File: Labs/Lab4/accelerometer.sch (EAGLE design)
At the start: 15 parts

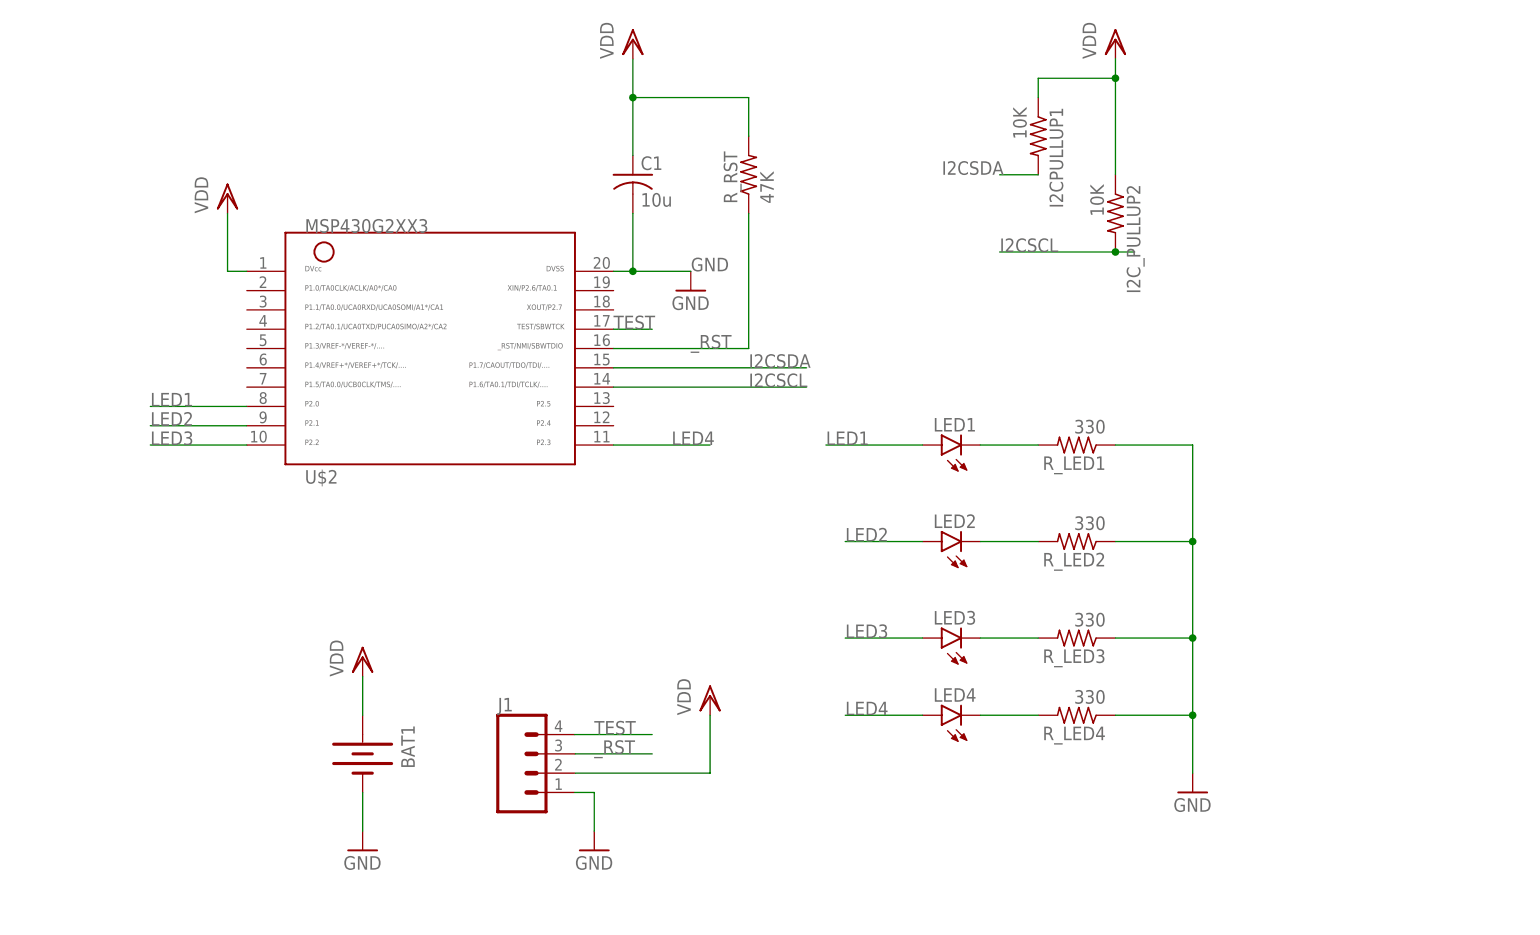
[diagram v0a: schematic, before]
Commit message: Fixed connections in Lab 4 schematic
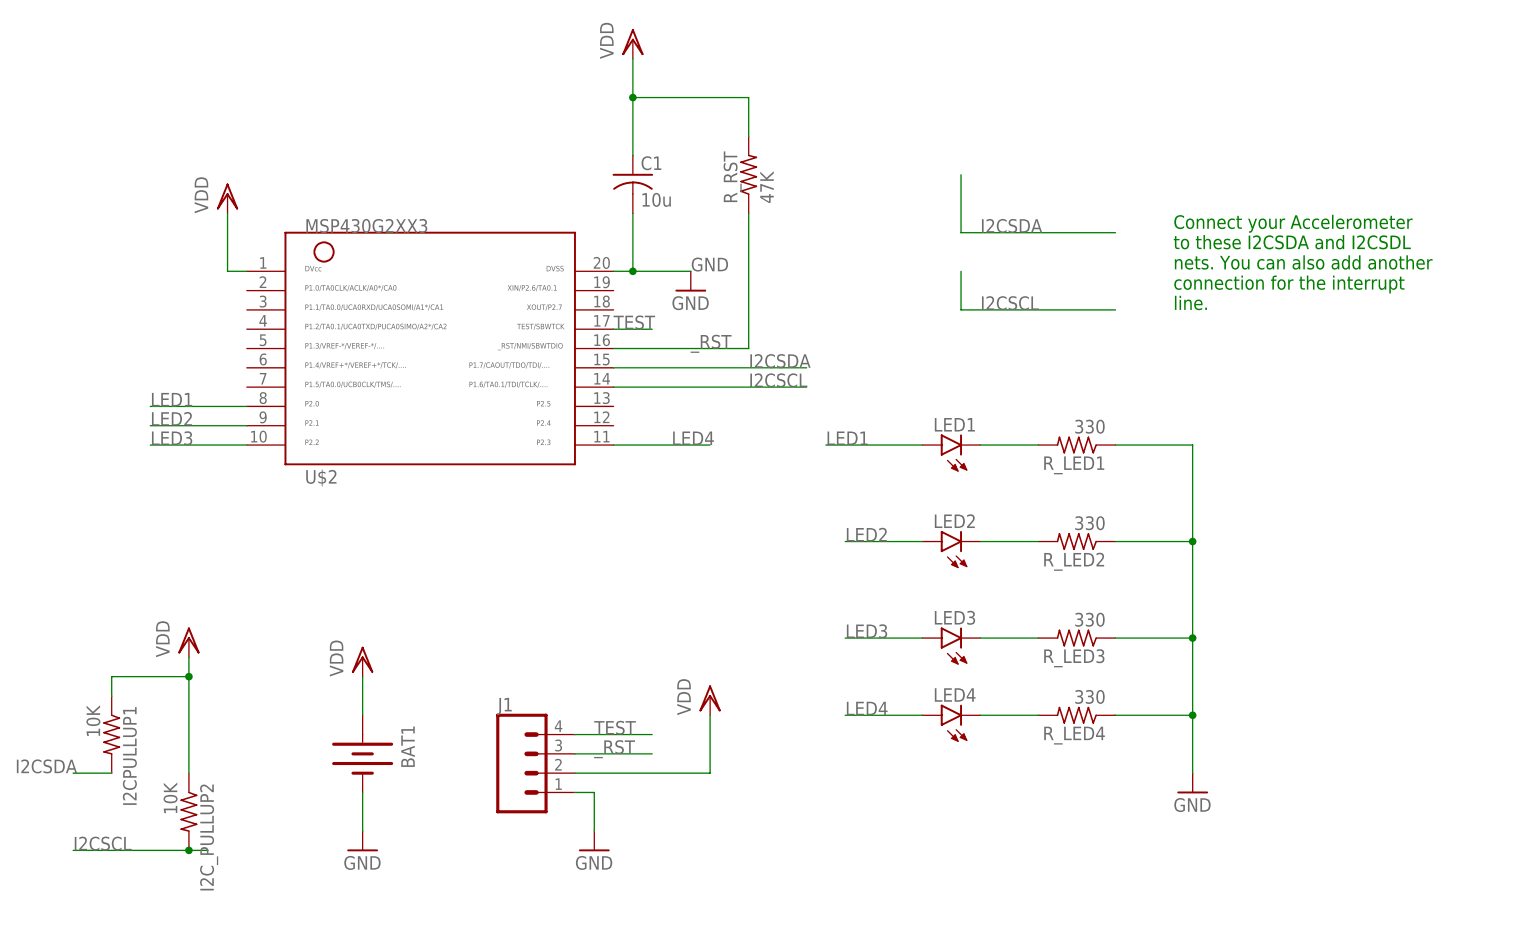
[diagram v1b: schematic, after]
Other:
- note added: "Connect your Accelerometer to these I2CSDA and I2CSDL nets. You can also add another connection for the interrupt line."
- moved on the sheet: I2CPULLUP1, I2C_PULLUP2
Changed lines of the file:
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@@
 <sheet>
 <plain>
+<text x="73.66" y="175.26" size="1.778" layer="91">Connect your Accelerometer
+to these I2CSDA and I2CSDL
+nets. You can also add another
+connection for the interrupt
+line.</text>
 </plain>
 <instances>
@@
 <attribute name="VALUE" x="73.66" y="109.22" size="1.778" layer="96"/>
 </instance>
-<instance part="I2CPULLUP1" gate="G$1" x="55.88" y="198.12" smashed="yes" rot="R270">
-<attribute name="NAME" x="57.3786" y="201.93" size="1.778" layer="95" rot="R270"/>
-<attribute name="VALUE" x="52.578" y="201.93" size="1.778" layer="96" rot="R270"/>
-</instance>
-<instance part="I2C_PULLUP2" gate="G$1" x="66.04" y="187.96" smashed="yes" rot="R270">
-<attribute name="NAME" x="67.5386" y="191.77" size="1.778" layer="95" rot="R270"/>
-<attribute name="VALUE" x="62.738" y="191.77" size="1.778" layer="96" rot="R270"/>
-</instance>
-<instance part="VDD4" gate="G$1" x="66.04" y="210.82" smashed="yes">
-<attribute name="VALUE" x="63.5" y="208.28" size="1.778" layer="96" rot="R90"/>
+<instance part="I2CPULLUP1" gate="G$1" x="-66.04" y="119.38" smashed="yes" rot="R270">
+<attribute name="NAME" x="-64.5414" y="123.19" size="1.778" layer="95" rot="R270"/>
+<attribute name="VALUE" x="-69.342" y="123.19" size="1.778" layer="96" rot="R270"/>
+</instance>
+<instance part="I2C_PULLUP2" gate="G$1" x="-55.88" y="109.22" smashed="yes" rot="R270">
+<attribute name="NAME" x="-54.3814" y="113.03" size="1.778" layer="95" rot="R270"/>
+<attribute name="VALUE" x="-59.182" y="113.03" size="1.778" layer="96" rot="R270"/>
+</instance>
+<instance part="VDD4" gate="G$1" x="-55.88" y="132.08" smashed="yes">
+<attribute name="VALUE" x="-58.42" y="129.54" size="1.778" layer="96" rot="R90"/>
 </instance>
 </instances>
@@
 <segment>
 <pinref part="I2CPULLUP1" gate="G$1" pin="1"/>
-<wire x1="55.88" y1="203.2" x2="55.88" y2="205.74" width="0.1524" layer="91"/>
-<wire x1="55.88" y1="205.74" x2="66.04" y2="205.74" width="0.1524" layer="91"/>
+<wire x1="-66.04" y1="124.46" x2="-66.04" y2="127" width="0.1524" layer="91"/>
+<wire x1="-66.04" y1="127" x2="-55.88" y2="127" width="0.1524" layer="91"/>
 <pinref part="VDD4" gate="G$1" pin="VDD"/>
-<wire x1="66.04" y1="205.74" x2="66.04" y2="208.28" width="0.1524" layer="91"/>
+<wire x1="-55.88" y1="127" x2="-55.88" y2="129.54" width="0.1524" layer="91"/>
 <pinref part="I2C_PULLUP2" gate="G$1" pin="1"/>
-<wire x1="66.04" y1="205.74" x2="66.04" y2="193.04" width="0.1524" layer="91"/>
-<junction x="66.04" y="205.74"/>
+<wire x1="-55.88" y1="127" x2="-55.88" y2="114.3" width="0.1524" layer="91"/>
+<junction x="-55.88" y="127"/>
 </segment>
 </net>
@@
 </segment>
 <segment>
-<wire x1="50.8" y1="193.04" x2="55.88" y2="193.04" width="0.1524" layer="91"/>
+<wire x1="-71.12" y1="114.3" x2="-66.04" y2="114.3" width="0.1524" layer="91"/>
 <pinref part="I2CPULLUP1" gate="G$1" pin="2"/>
-<label x="43.18" y="193.04" size="1.778" layer="95"/>
+<label x="-78.74" y="114.3" size="1.778" layer="95"/>
+</segment>
+<segment>
+<wire x1="66.04" y1="185.42" x2="45.72" y2="185.42" width="0.1524" layer="91"/>
+<wire x1="45.72" y1="185.42" x2="45.72" y2="193.04" width="0.1524" layer="91"/>
+<label x="48.26" y="185.42" size="1.778" layer="95"/>
 </segment>
 </net>
@@
 </segment>
 <segment>
-<wire x1="50.8" y1="182.88" x2="66.04" y2="182.88" width="0.1524" layer="91"/>
+<wire x1="-71.12" y1="104.14" x2="-55.88" y2="104.14" width="0.1524" layer="91"/>
 <pinref part="I2C_PULLUP2" gate="G$1" pin="2"/>
-<wire x1="66.04" y1="182.88" x2="68.58" y2="182.88" width="0.1524" layer="91"/>
-<junction x="66.04" y="182.88"/>
-<label x="50.8" y="182.88" size="1.778" layer="95"/>
+<wire x1="-55.88" y1="104.14" x2="-53.34" y2="104.14" width="0.1524" layer="91"/>
+<junction x="-55.88" y="104.14"/>
+<label x="-71.12" y="104.14" size="1.778" layer="95"/>
+</segment>
+<segment>
+<wire x1="66.04" y1="175.26" x2="45.72" y2="175.26" width="0.1524" layer="91"/>
+<wire x1="45.72" y1="175.26" x2="45.72" y2="180.34" width="0.1524" layer="91"/>
+<label x="48.26" y="175.26" size="1.778" layer="95"/>
 </segment>
 </net>
@@
 </drawing>
 <compatibility>
+<note version="6.3" minversion="6.2.2" severity="warning">
+Since Version 6.2.2 text objects can contain more than one line,
+which will not be processed correctly with this version.
+</note>
 <note version="8.2" severity="warning">
 Since Version 8.2, EAGLE supports online libraries. The ids
